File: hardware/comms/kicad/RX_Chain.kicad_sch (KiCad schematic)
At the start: 40 parts, among them Q4 2SC3356, U10 ADE-1+, U5 MCP6022, U9 PSA4-5043+

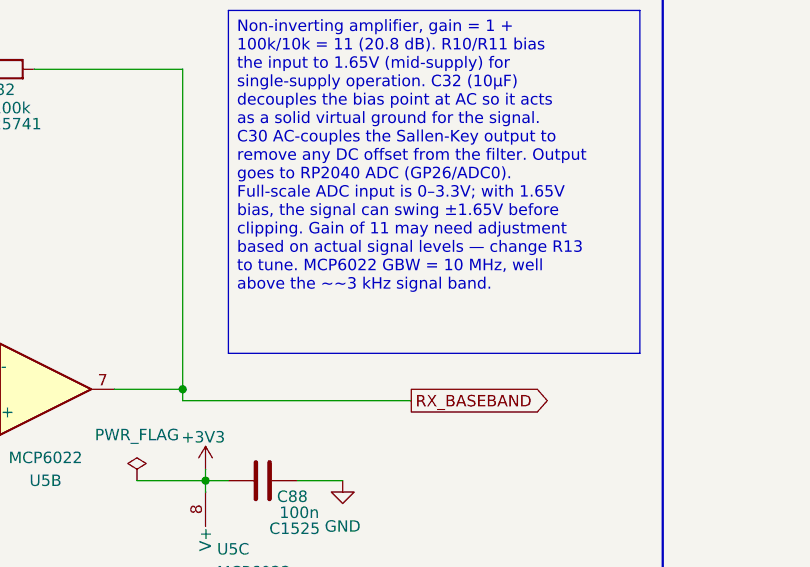
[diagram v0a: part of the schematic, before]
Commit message: comms/kicad: rename project and sheets, correct schematic text
  Renames
  - transciever_kicad.{pro,sch,pcb} -> transceiver.{pro,sch,pcb}: the
    project name was misspelled, and the _kicad suffix was redundant
    inside a kicad/ directory.
  - Sheet files lose their spaces: Clock_Gen, Digital_Control, RX_Chain,
    TX_Chain. Sheetname keeps its space -- that is the label drawn on the
    sheet, not a path.
  - References updated in four places, not one: 4 Sheetfile properties in
    the root schematic, 186 per-symbol (project ...) instances across every
    sheet, 68 per-footprint (sheetfile ...) entries in the PCB, and
    meta.filename plus the root sheet name in the project file. Verified
    afterwards that all sheet references resolve, no sheet is orphaned, and
    the project file still parses.

  Spelling and stale labels
  - Title block: Revsion -> Revision, Repsoitory -> Repository, repository
    path centisat -> ember, project named EMBER.
  - PCI-104 -> CSKB in three files. PCI-104 is a different real standard,
    and the same sheet's own revision history records the bus being renamed
    to CSKB back at rev 0.4.
  - Status LED's -> Status LEDs; +20 db -> +20 dB; RX SMA < - -> <-.
  - The tripler note named BRF92A as the flight transistor: misspelled, and
    superseded by the 2SC3356 actually placed. Corrected to 2SC3356 with
    the MMBT3904-footprint note the implementation plan records. The
    ft=5 GHz figure is dropped rather than reassigned to a part it was not
    measured against.
  - Power sheet: the D4 forward-drop note referred to the SA612, replaced
    by the ADE-1+ back at rev 0.5. Now names the PSA4-5043+.
 Altium-to-KiCad text damage
  Three separate corruptions, classified before replacing so that real
  values were not caught up in it -- ~21 dB and ~20 dB both contain a
  literal ~2 and would have been mangled by a blind pass.
  - 144 table column separators rendered as literal ~2; now |, so the
    sheet index, rail summary, net c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
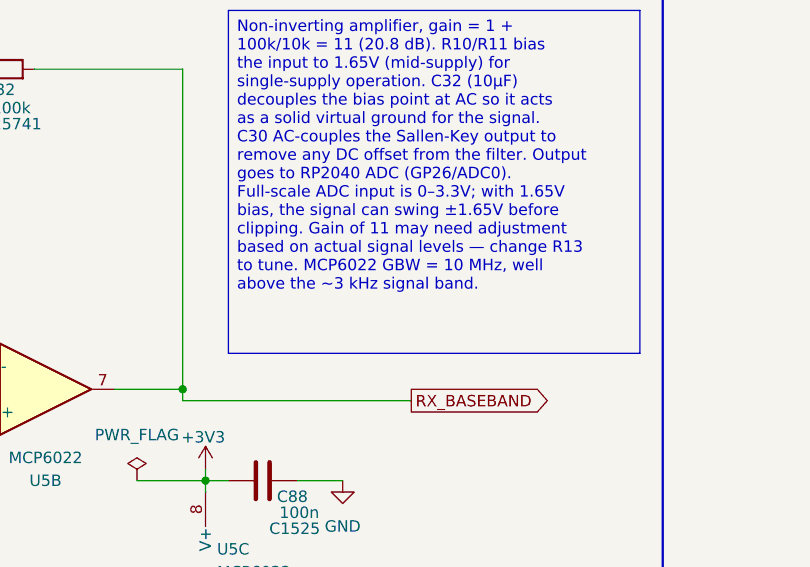
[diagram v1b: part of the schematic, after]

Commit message: comms: checkpoint current KiCad design before ground station work
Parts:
- added R38, R39: 100k, Resistor_SMD:R_0402_1005Metric, symbol Device:R
- C75: value C -> 100n; footprint (none) -> Capacitor_SMD:C_0402_1005Metric; LCSC Part # (none) -> C1525; Manufacturer Part # (none) -> CL05B104KO5NNNC
- C82: value 8.2p -> 100n; LCSC Part # C1579 -> C1525; Manufacturer Part # (none) -> CL05B104KO5NNNC
- C83: LCSC Part # XXX -> C53547; Manufacturer Part # XXX -> 0402CG102J500NT
- C85: value 100n -> 8.2p; LCSC Part # C1525 -> C1579; Manufacturer Part # CL05B104KO5NNNC -> (none)
- L16: value 1u -> 220n; footprint Inductor_SMD:L_0805_2012Metric -> Ember_RF:L_Coilcraft_0805HP; LCSC Part # C18221300 -> (none); MPN (none) -> 0805HP-221XJRC; Manufacturer (none) -> Coilcraft; Manufacturer Part # (none) -> 0805HP-221XJRC; PinMapAudit (none) -> design/l16_footprint_acceptance.md; Qualification (none) -> Prototype; RF bench qualification pending
- Q4: symbol Simulation_SPICE:NPN -> Transistor_BJT:Q_NPN_BEC; Manufacturer (none) -> Guangdong Hottech; Manufacturer Part # (none) -> 2SC3356
- U10: LCSC Part # (none) -> C2942210; MPN (none) -> ADE-1+; Manufacturer (none) -> Mini-Circuits; Manufacturer Part # (none) -> ADE-1+; Package (none) -> CD636; PackageHeightMax_mm (none) -> 4.11; PinMapAudit (none) -> design/u10_ade1_pinmap.md
- U5: footprint (none) -> Package_SO:SOIC-8_3.9x4.9mm_P1.27mm; LCSC Part # (none) -> C57639; MPN (none) -> MCP6022-I/SN; Manufacturer (none) -> Microchip Technology; Manufacturer Part # (none) -> MCP6022T-I/SN
- U9: footprint Package_TO_SOT_SMD:SOT-343_SC-70-4 -> Ember_RF:PSA4-5043_MMM1362; symbol RF_Amplifier:SPF5189Z -> Ember_RF:PSA4-5043+; MPN (none) -> PSA4-5043+; Manufacturer (none) -> Mini-Circuits
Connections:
- net GND: now also Q4.2 (E), U9.4 (GND); no longer Q4.3 (E), R30.2
- net RX_IF: now also R38.1
- net RX_AMP_IN: now reaches C69.1, U5.5 (+)
- net RX_AMP_IN: now also R39.2; no longer C72.2
- net VREF_RX: now reaches R28.2, R29.1
- net VREF_RX: now also C72.2, R30.2, R38.2, R39.1
- net at C85.1, C86.1, L18.2: now also Q4.3 (C); no longer Q4.1 (C)
- net at C83.1, R33.1: now also Q4.1 (B); no longer Q4.2 (B)
- net at C75.1, L16.2: now also U9.1 (OUT_DC); no longer U9.3
- net at C67.2: now also U9.3 (IN); no longer U9.1

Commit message: Complete dual-CAN transceiver hardware prototype
Preserve the current transceiver schematics, PCB, libraries and validation evidence as a focused hardware review against main.
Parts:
- C99: footprint Capacitor_SMD:C_0402_1005Metric -> Capacitor_SMD:C_0805_2012Metric; LCSC Part # C1525 -> C1711; MPN (none) -> CL21B104KBCNNNC; Manufacturer (none) -> Samsung Electro-Mechanics; Manufacturer Part # CL05B104KO5NNNC -> CL21B104KBCNNNC
- L12, L13, L20, L22: LCSC Part # C40976557 -> C90642; MPN (none) -> LQW15AN10NG00D; Manufacturer (none) -> Murata Electronics
- L16: LCSC Part # (none) -> C40877572; MPN 0805HP-221XJRC -> 0805HP-221XGRC; Manufacturer Part # 0805HP-221XJRC -> 0805HP-221XGRC; PinMapAudit design/l16_footprint_acceptance.md -> verification/components/l16_footprint_acceptance.md; Qualification Prototype; RF bench qualification pending -> Prototype selection; see verification/components/prototype_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
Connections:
- net RX_AMP_IN: no longer names the net of C69.1, R39.2, U5.5 (+)
- net VREF_RX: no longer names the net of C72.2, R28.2, R29.1, R30.2, R38.2, R39.1
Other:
- moved on the sheet: C72, R28, R29, R30, R32, R38, R39
